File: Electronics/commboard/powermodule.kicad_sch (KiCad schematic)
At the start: 12 parts, among them J501 InputConn, U501 LM2576HVS-3.3

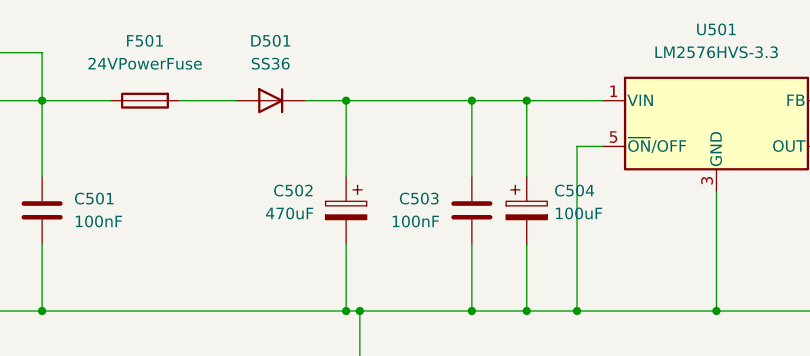
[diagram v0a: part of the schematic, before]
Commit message: schematic design completed. pcb layout drawings completed.
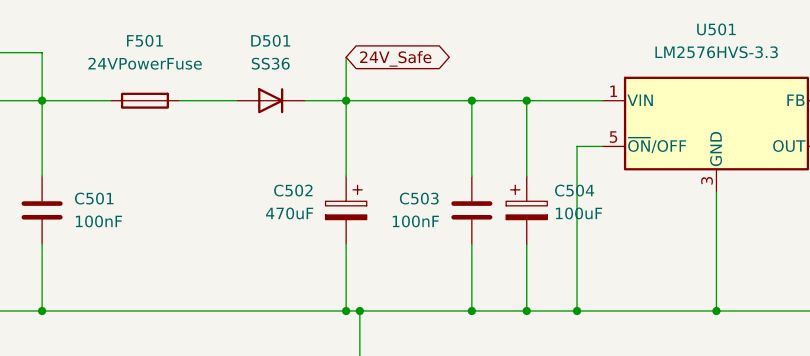
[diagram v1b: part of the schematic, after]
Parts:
- C503: footprint Capacitor_THT:CP_Radial_D5.0mm_P2.50mm -> Capacitor_THT:C_Rect_L7.0mm_W2.5mm_P5.00mm
- J501: footprint Connector_PinHeader_2.54mm:PinHeader_1x02_P2.54mm_Vertical -> Connector_Phoenix_MSTB:PhoenixContact_MSTBVA_2,5_2-G-5,08_1x02_P5.08mm_Vertical
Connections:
- net 24V_Safe: now reaches C502.1, C503.1, C504.1, D501.1 (K), U501.1 (VIN)
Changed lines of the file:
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@@
+    (stroke (width 0) (type default) (color 0 0 0 0))
+  )
+  (wire (pts (xy 150.876 67.818) (xy 150.876 72.644))
     (stroke (width 0) (type default) (color 0 0 0 0))
   )
@@
   (wire (pts (xy 192.024 96.012) (xy 214.884 96.012))
     (stroke (width 0) (type default) (color 0 0 0 0))
+  )
+  (global_label "24V_Safe" (shape bidirectional) (at 150.876 67.818 0) (fields_autoplaced)
+    (effects (font (size 1.27 1.27)) (justify left))
+    (property "Intersheet References" "${INTERSHEET_REFS}" (id 0) (at 161.9372 67.7386 0)
+      (effects (font (size 1.27 1.27)) (justify left) hide)
+    )
   )
   (hierarchical_label "GND" (shape input) (at 152.4 102.616 0)
@@
       (effects (font (size 1.27 1.27)) (justify left))
     )
-    (property "Footprint" "Connector_PinHeader_2.54mm:PinHeader_1x02_P2.54mm_Vertical" (id 2) (at 105.918 72.644 0)
+    (property "Footprint" "Connector_Phoenix_MSTB:PhoenixContact_MSTBVA_2,5_2-G-5,08_1x02_P5.08mm_Vertical" (id 2) (at 105.918 72.644 0)
       (effects (font (size 1.27 1.27)) hide)
     )
@@
       (effects (font (size 1.27 1.27)) (justify right))
     )
-    (property "Footprint" "Capacitor_THT:CP_Radial_D5.0mm_P2.50mm" (id 2) (at 165.8112 88.646 0)
-      (effects (font (size 1.27 1.27)) hide)
-    )
+    (property "Footprint" "Capacitor_THT:C_Rect_L7.0mm_W2.5mm_P5.00mm" (id 2) (at 165.8112 88.646 0)
+      (effects (font (size 1.27 1.27)) hide)
+    )
